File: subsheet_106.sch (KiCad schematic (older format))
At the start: 47 parts, among them Q100 2N3904, Q101 2N3904, Q102 2N3904, Q103 2N3904, Q104 2N3904, U402 32.215905 MHz (NTSC) — 32.084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, Y100 4.433618MHz, Y101 32.084988MHz

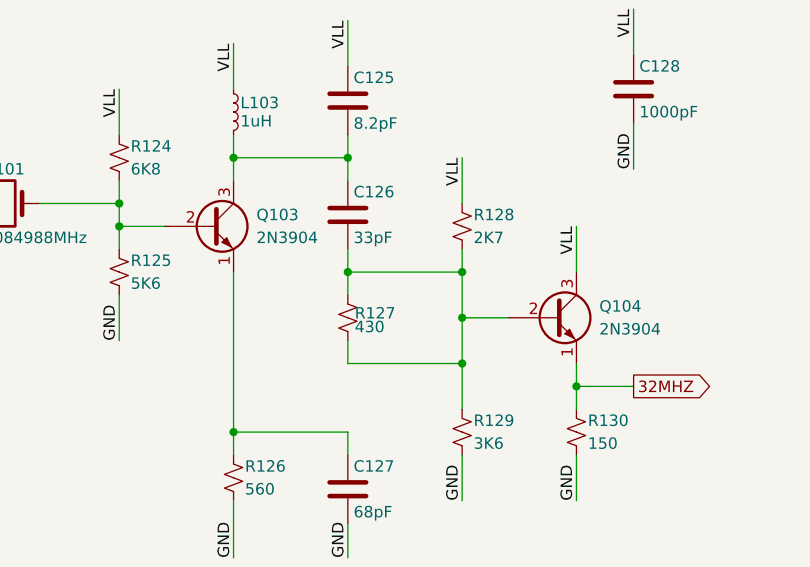
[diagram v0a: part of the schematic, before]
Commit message: Fixed : R127 is shorted
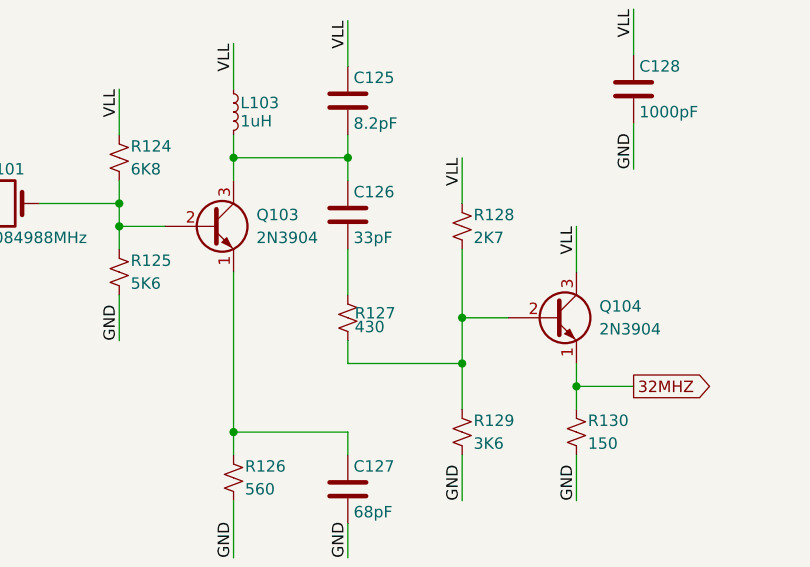
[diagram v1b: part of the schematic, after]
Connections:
- net at Q104.2 (B), R127.2, R128.2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: no longer C126.2, R127.1
- new net: C126.2, R127.1
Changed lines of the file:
@@
 	5750 7300 5750 7400
-Wire Wire Line
-	5750 7700 5750 7800
 Wire Wire Line
 	5750 8100 5750 8200
 Wire Wire Line
 	6250 7300 6250 7500
-Wire Wire Line
-	6250 7700 6250 7800
-Wire Wire Line
-	5750 7800 6250 7800
-Connection ~ 5750 7800
-Wire Wire Line
-	5750 7800 5750 7900
-Connection ~ 6250 7800
 Wire Wire Line
 	6250 8000 6450 8000
@@
 	6250 8000 6250 8200
 Wire Wire Line
-	6250 7800 6250 8000
+	5750 7700 5750 7900
+Wire Wire Line
+	6250 7700 6250 8000
 $EndSCHEMATC
